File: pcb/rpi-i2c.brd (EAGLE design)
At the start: 28 x 56 mm, 14 parts, among them IC1 DS2482-100, J2 CONN_05X2

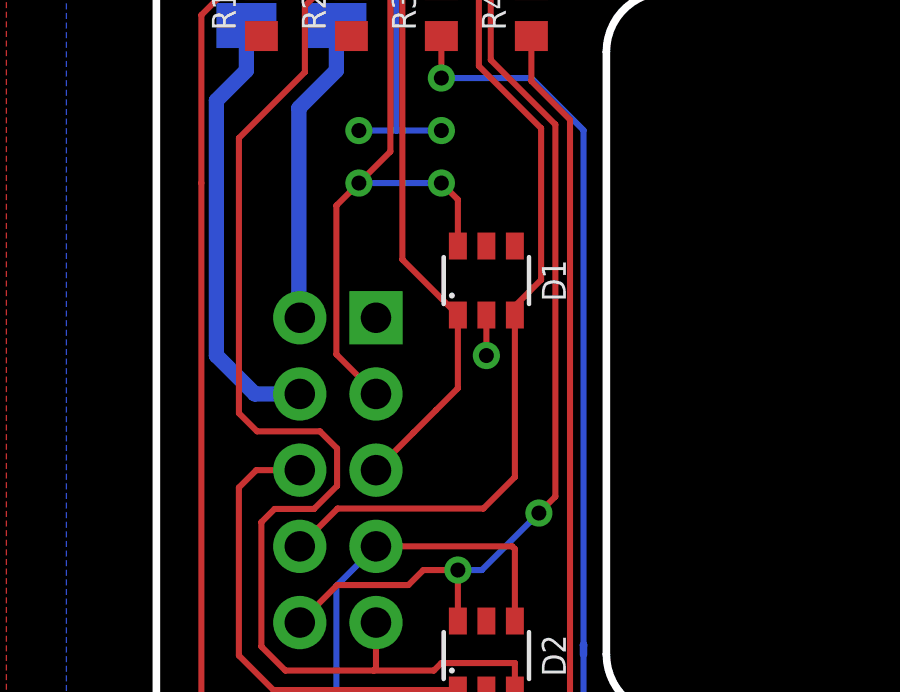
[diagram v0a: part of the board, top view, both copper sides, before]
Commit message: Clean up schematics and save PCB image.
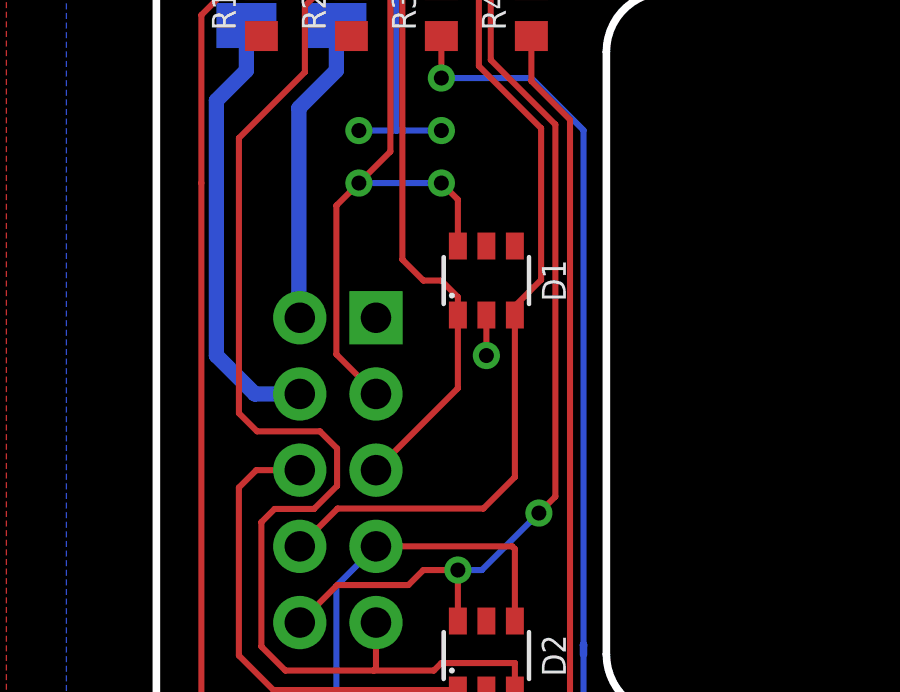
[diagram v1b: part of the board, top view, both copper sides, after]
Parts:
- J1: value (none) -> RPI
- J2: value CONN_05X2 -> EXT
